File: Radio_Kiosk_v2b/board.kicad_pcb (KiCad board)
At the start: 2 copper layers, 84 x 141 mm, 239 parts, among them J1 USB-C PD in, J11 UART, J12 USB-C, J13 Lid LEDs, J2 DC in 18-26V, PJ-002BH 5.5x2.5, J3 Laptop out 15.6V, PJ-002BH 5.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, J5 RJ45 radio, J6 RJ45 laptop, J8 Fan 12V, J9 SWD, Q1 SI4470EY, Q10 2N7002, Q11 AO3400A, Q12 SI4470EY, Q13 AO4482, Q2 SI4470EY, Q20 AO4482, Q22 PSMN075-100MSEX, Q23 DMP10H400SE, Q24 BSS123, Q25 2N7002, Q30 AO3400A, Q40 AOD4184A, Q41 AOD4184A, Q44 SI4401DDY, Q45 2N7002, Q6 SI4470EY, Q7 SI4470EY, Q8 AOD4185, Q9 2N7002, SW1 RESET, SW2 BOOT0 (DFU), U1 LM74700-Q1, U10 TLV7011, U12 LM74700-Q1, U2 LM74700-Q1, U20 LM3478 54V boost, U21 TPS26600 eFuse, U22 LTC4279, U3 LMR33630 12V, U30 SN74AHCT1G125, U31 SN74AHCT1G125, U4 LM3150 15.75V 4.5A, U40 STM32F072CBT6, U41 INA180A1, U42 INA180A1, U43 MCP6001T-I/OT, U45 TLV7011, U5 LMR33630 5V, U50 CH224A, U51 AP2112K-3.3, U52 USBLC6-2SC6, U6 LM74700-Q1, U7 LM74700-Q1

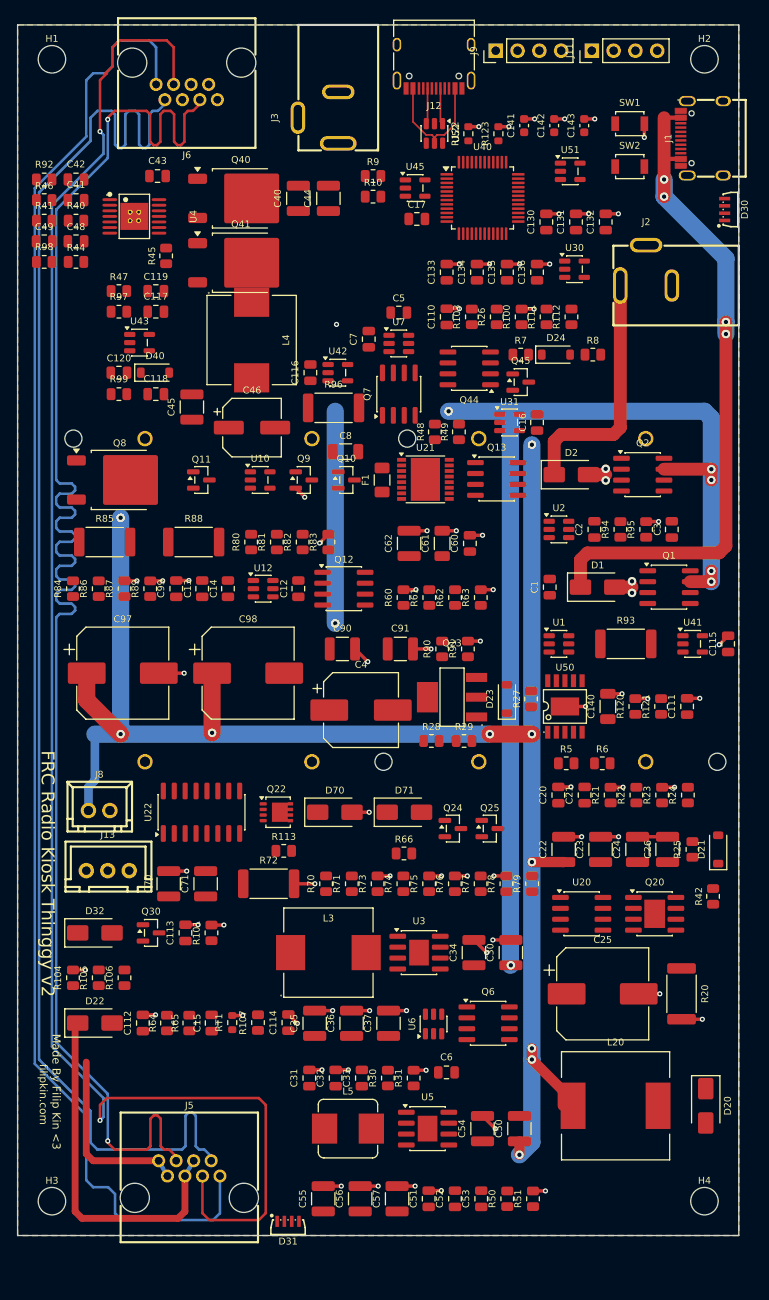
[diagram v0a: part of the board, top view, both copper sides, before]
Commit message: v2b: laptop corner respaced for routing lanes; every silk label placed clear
Left strip one column with lanes, CC loop in rows with label room, EN and
PWM-filter resistors moved to the free band; D40 off the battery pin; FET
pair and input caps up 0.5 mm, L4 down 0.4 mm. tools/labels.py put all 239
labels just outside their parts, clear of pads, parts and other labels:
DRC silk_overlap 110 -> 0, silk_over_copper 84 -> 0 (C33's label is 0.7 mm).

Co-Authored-By: Claude Opus 5.5 (1M context) <noreply@anthropic.com>
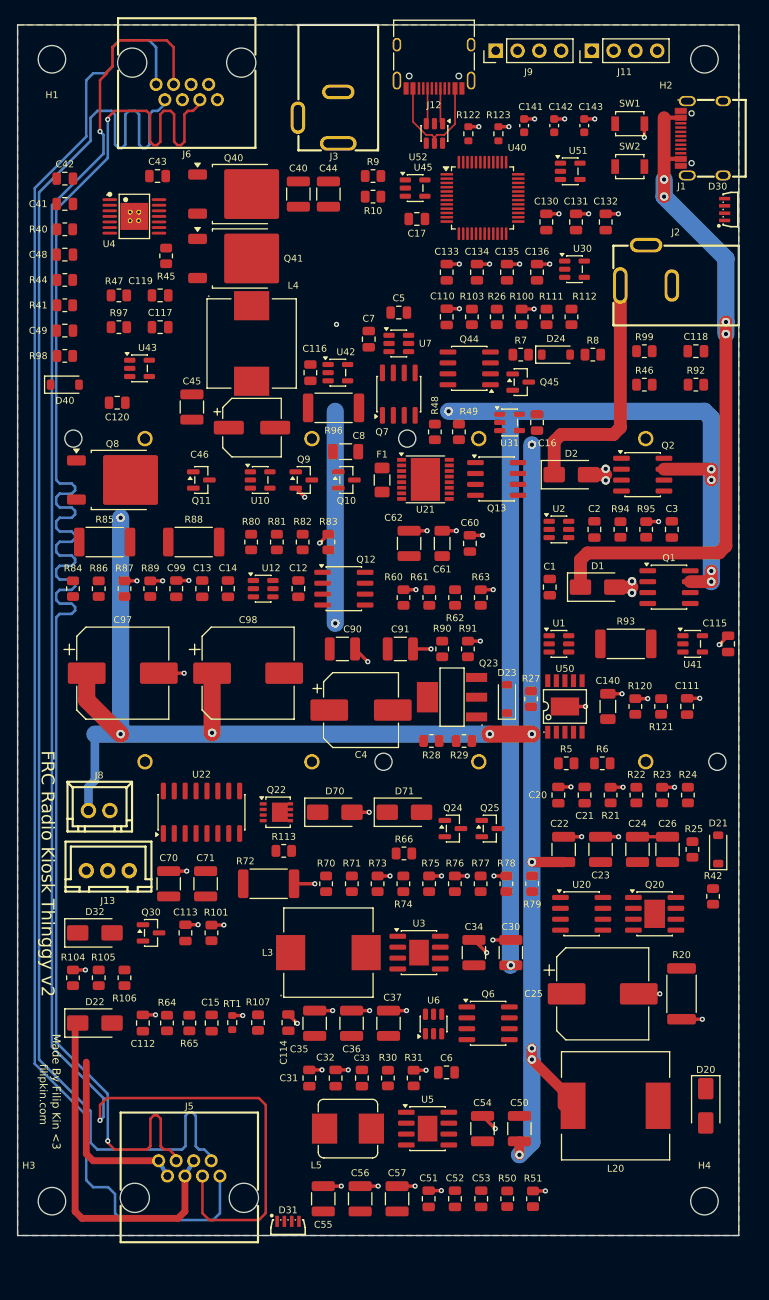
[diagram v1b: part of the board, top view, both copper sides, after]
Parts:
- moved R92 79.6 mm to (79.0, 41.9)
- moved R46 73.1 mm to (73.0, 41.9)
- moved C118 63.1 mm to (79.0, 38.0)
- moved R99 61.4 mm to (73.0, 38.0)
- moved R98 11.2 mm to (5.50, 38.5)
- moved C49 10.7 mm to (5.50, 35.6)
- moved D40 10.6 mm to (5.50, 41.9)
- moved R41 10.1 mm to (5.50, 32.6)
- moved C120 3.51 mm to (11.6, 44.0)
- moved U43 3.00 mm to (14.2, 40.0)
- moved R44 2.47 mm to (5.50, 29.7)
- moved C48 2.02 mm to (5.50, 26.8)
- moved C117 1.87 mm to (16.6, 35.2)
- moved R97 1.80 mm to (11.8, 35.2)
- moved R40 1.64 mm to (5.50, 23.8)
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
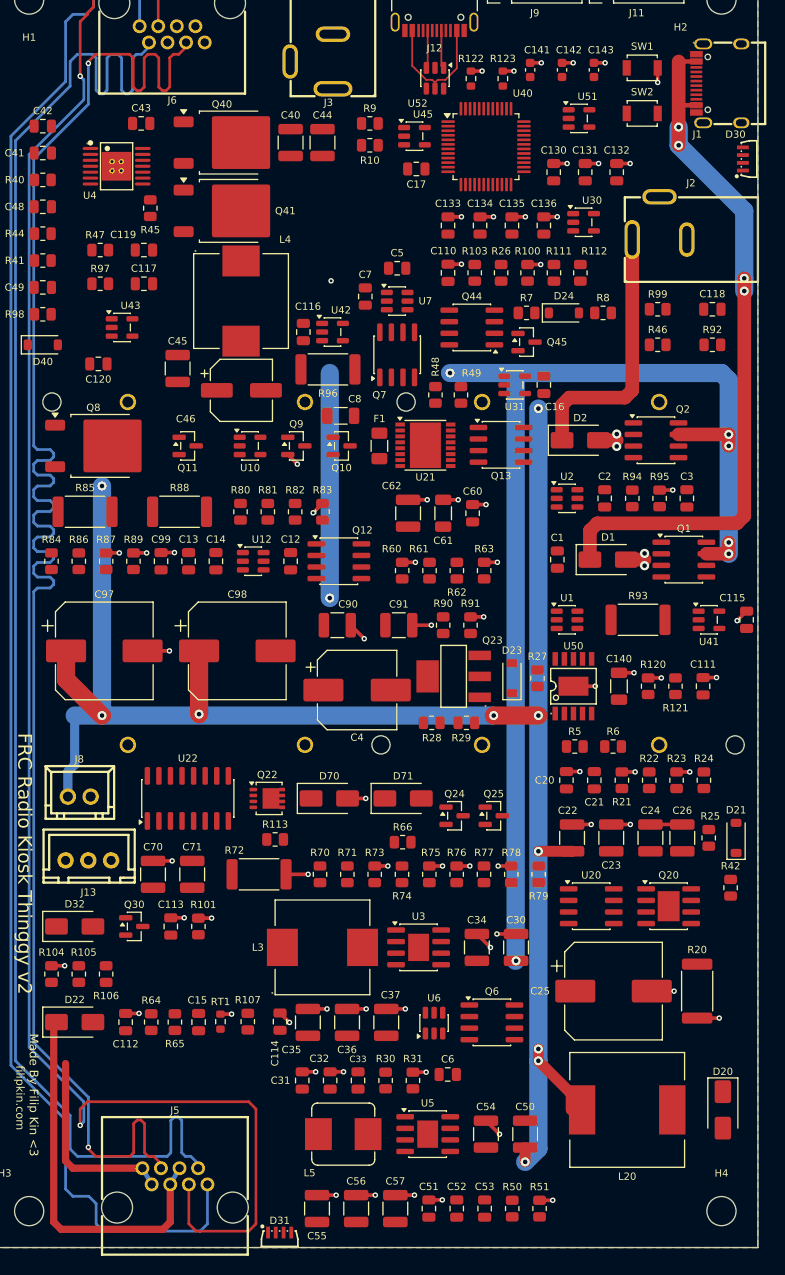
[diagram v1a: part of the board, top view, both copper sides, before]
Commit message: v2b: front pour GND, back pour +12V
Back zone moved to +12V (Filip). GND stitching vias that only joined front
ground to the old back ground pour are gone (72). 18 front +12V pads got a
0.4 mm stub + via to the back pour (tools/netvias.py); U52's ground pin,
boxed in by the USB traces, joins the main ground through a via pair and a
short back jumper. Pours filled with KiCad's filler. Refilled DRC: GND one
island, +12V open only at U21.3 and Q8.2 (to route), GND open at U40.8,
U40.35, U1.2, U2.2 (pins between signal pins), errors only J1's pad gaps.

Co-Authored-By: Claude Opus 5.5 (1M context) <noreply@anthropic.com>
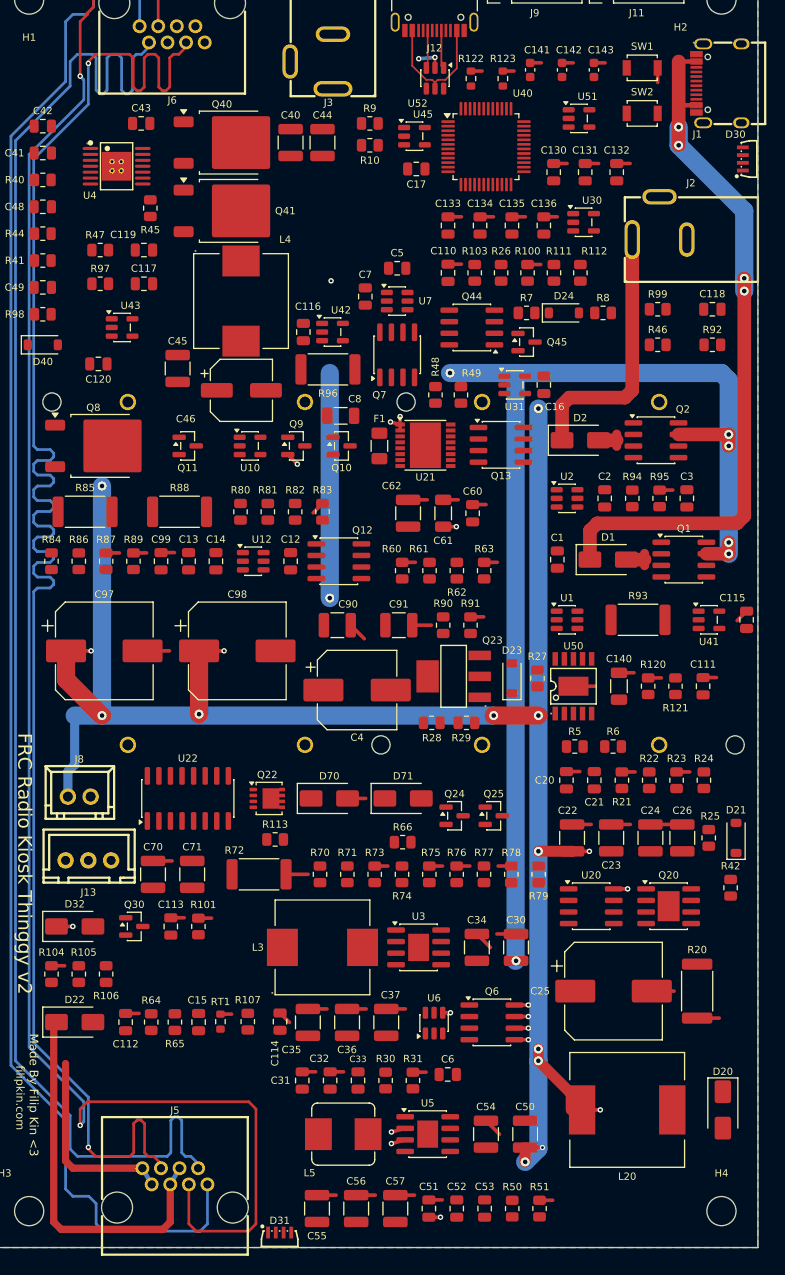
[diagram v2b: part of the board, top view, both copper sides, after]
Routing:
- net +12V: track 197.8 -> 227.8 mm, vias 10 -> 28
- net GND: track 123.3 -> 126.2 mm, vias 72 -> 2
- added copper zone on B.Cu, net +12V
- removed copper zone on B.Cu, net GND

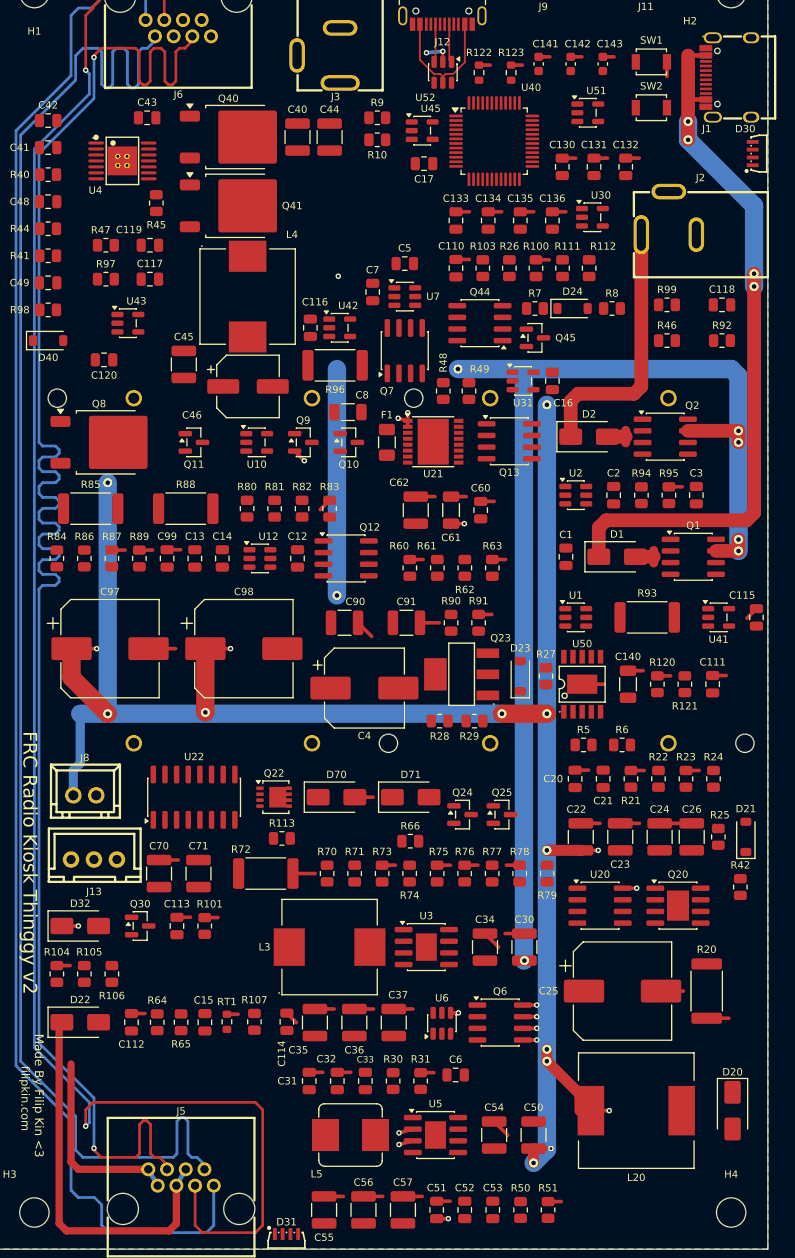
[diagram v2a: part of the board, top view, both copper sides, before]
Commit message: v2b: dead copper removed now that both sides are planes
73 GND stubs with a free end (old stitch stubs; the pads sit in the front
GND pour), the D1/D2 return stubs and via bars, a no-net back track with its
via, dead +3V3 and BK_ARM vias, and 13 +12V stub vias on pads that already
reach +12V. Q6's four drain vias -> pins tied + two 1.0/0.5 vias (3 A);
U21 IN pins tied to one 0.8/0.4 via; U5 VIN/EN tied to one via. U52's ground
jumper stays (boxed in by the USB traces). Pours refilled. DRC: errors only
J1's pad gaps, silk clean, GND one island.

Co-Authored-By: Claude Opus 5.5 (1M context) <noreply@anthropic.com>
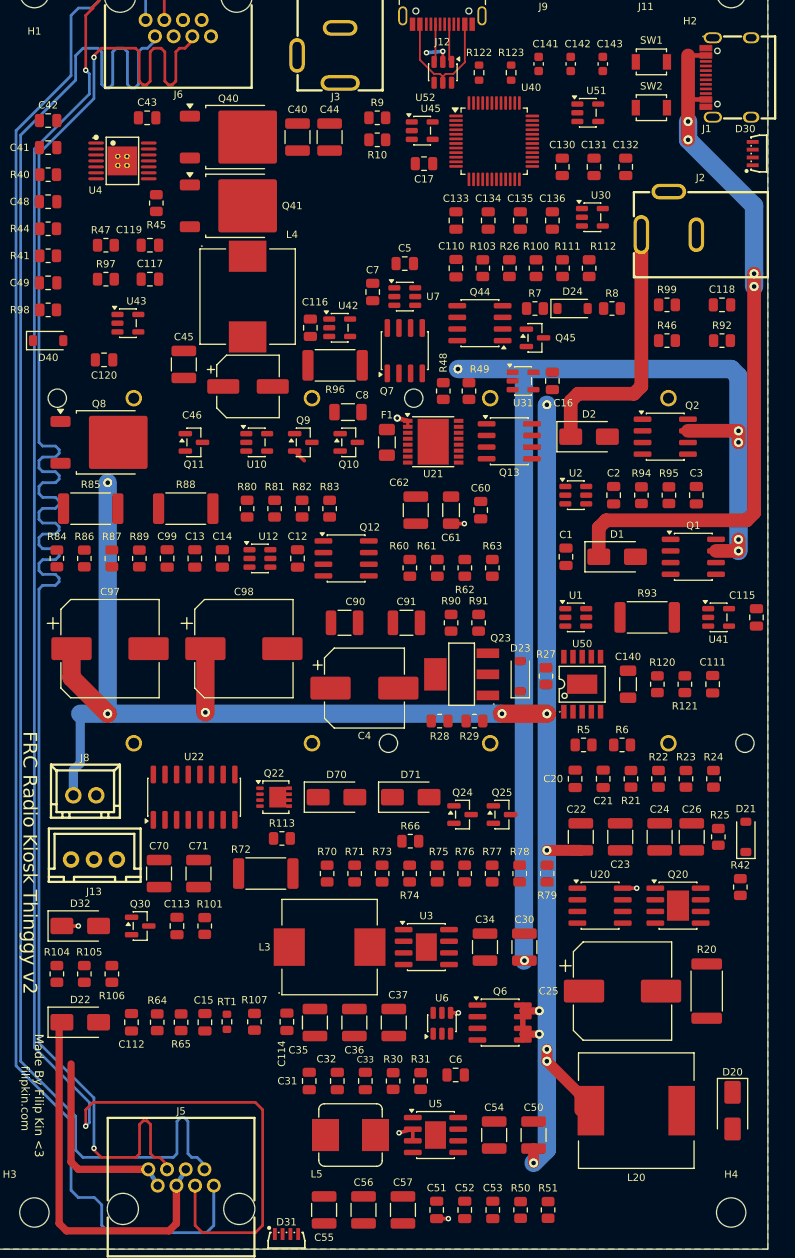
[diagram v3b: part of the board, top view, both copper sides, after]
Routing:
- net GND: track 126.2 -> 2.94 mm
- net (no net): track 24.7 -> 0.00 mm, vias 1 -> 0
- net +12V: track 227.8 -> 216.7 mm, vias 28 -> 19
- net BK_ARM: vias 1 -> 0
- net +3V3: vias 1 -> 0

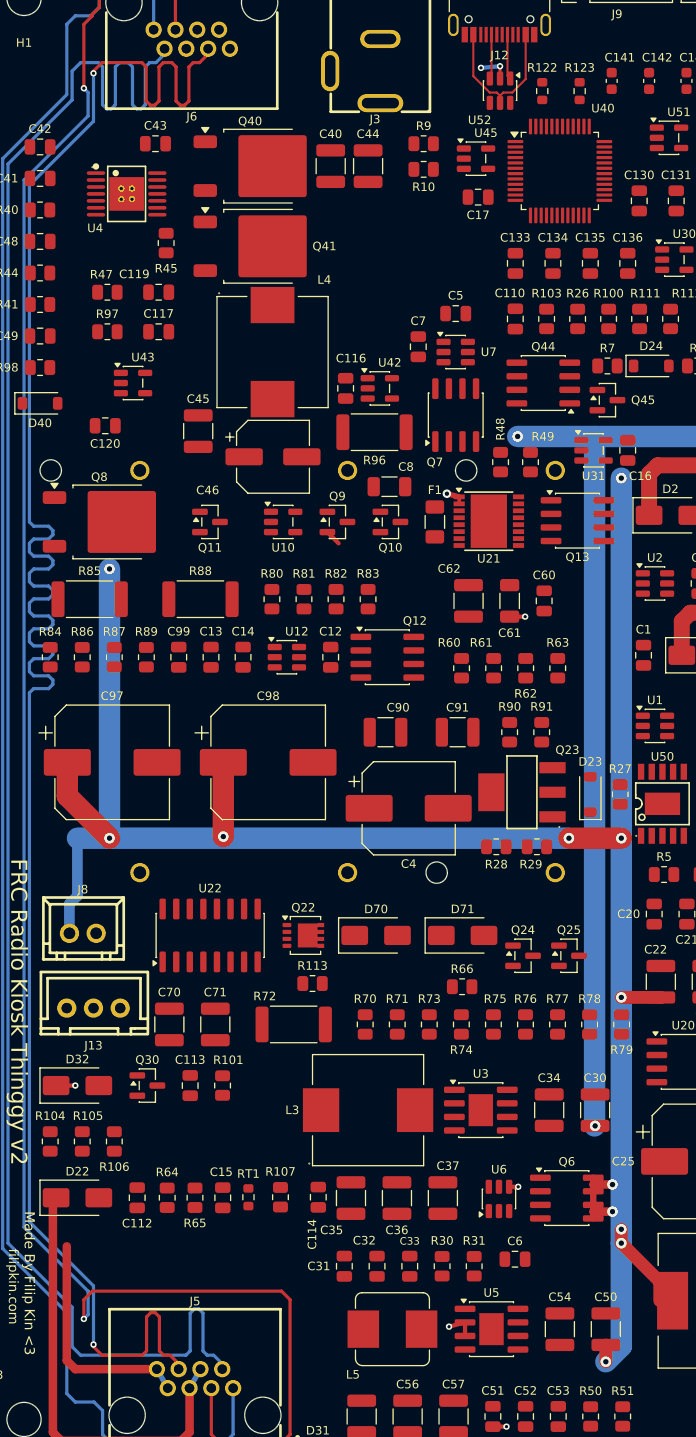
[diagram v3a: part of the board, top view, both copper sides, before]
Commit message: v2b: back +12V tracks removed (the pour carries it), PC14 net restored, U52 ground jumper into the main pour
8 B.Cu +12V segments were redundant under the +12V back pour. U40 pin 3
(PC14, LAPTOP_BYP) had no net on the board though the schematic has one: the
pad-net pass had skipped pads with no net field. The U52 ground jumper's far
via sat in a second pocket inside the VBUS loop; moved to (45, 11.4) in the
main pour. Refilled; DRC errors only J1's pad gaps; GND and +12V pours each
one piece; silk clean.

Co-Authored-By: Claude Opus 5.5 (1M context) <noreply@anthropic.com>
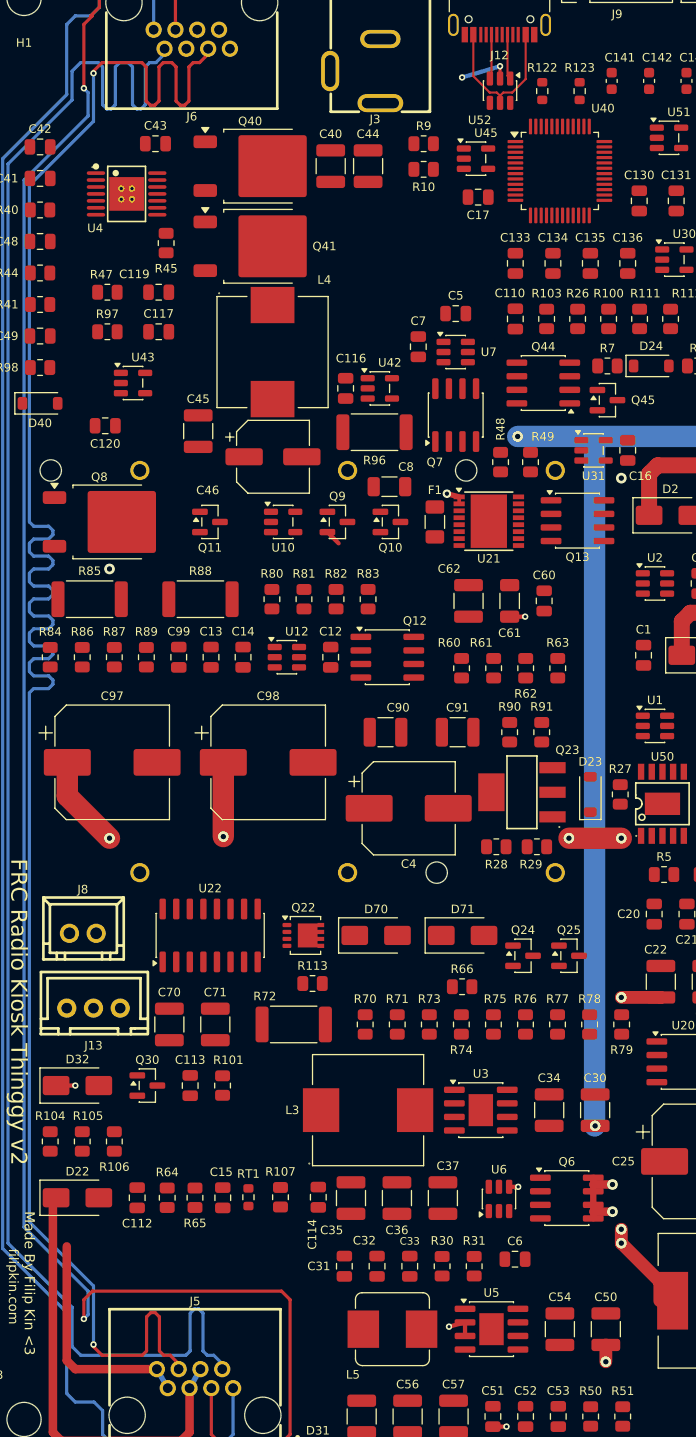
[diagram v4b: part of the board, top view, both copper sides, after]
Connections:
- U40 pad 3: (no net) -> LAPTOP_BYP
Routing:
- net +12V: track 216.7 -> 53.0 mm
- net GND: track 2.94 -> 4.85 mm
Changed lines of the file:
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@@
 			(layers "F.Cu" "F.Mask" "F.Paste")
 			(roundrect_rratio 0.25)
+			(net "LAPTOP_BYP")
 		)
 		(pad "4" smd roundrect
@@
 	)
 	(via
-		(at 46.768 10.5)
+		(at 45 11.4)
 		(size 0.6)
 		(drill 0.3)
@@
 	(segment
 		(start 48.55 10.35)
-		(end 46.768 10.5)
+		(end 45 11.4)
 		(width 0.4)
 		(layer "B.Cu")
@@
 		(net "+12V")
 	)
-	(segment
-		(start 9 82.6)
-		(end 9 88)
-		(width 1)
-		(layer "B.Cu")
-		(net "+12V")
-	)
-	(segment
-		(start 55 82.6)
-		(end 9 82.6)
-		(width 2)
-		(layer "B.Cu")
-		(net "+12V")
-	)
-	(segment
-		(start 59.9 120.5)
-		(end 59.9 48.9)
-		(width 2)
-		(layer "B.Cu")
-		(net "+12V")
-	)
-	(segment
-		(start 8.25 88.75)
-		(end 8.25 91.5)
-		(width 1)
-		(layer "B.Cu")
-		(net "+12V")
-	)
-	(segment
-		(start 12 82.6)
-		(end 12 57.4)
-		(width 2)
-		(layer "B.Cu")
-		(net "+12V")
-	)
-	(segment
-		(start 59.9 120.5)
-		(end 59.9 130.15)
-		(width 2)
-		(layer "B.Cu")
-		(net "+12V")
-	)
-	(segment
-		(start 59.9 130.15)
-		(end 58.45 131.6)
-		(width 2)
-		(layer "B.Cu")
-		(net "+12V")
-	)
-	(segment
-		(start 9 88)
-		(end 8.25 88.75)
-		(width 1)
-		(layer "B.Cu")
-		(net "+12V")
-	)
